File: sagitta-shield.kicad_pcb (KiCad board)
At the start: 2 copper layers, 29.2 x 91.6 mm, 53 parts, among them J1 EADC1, J10 SENSGND, J11 POWER, J2 EADC2, J3 MicroSD, J4 RTD, J5 IADC, J6 SWITCH, J7 UART2, J8 I2C, J9 SENSVDD, Q1 BSS84, U1 MAX31865, U2 ADS1115IDGS, U3 A1104LLHL

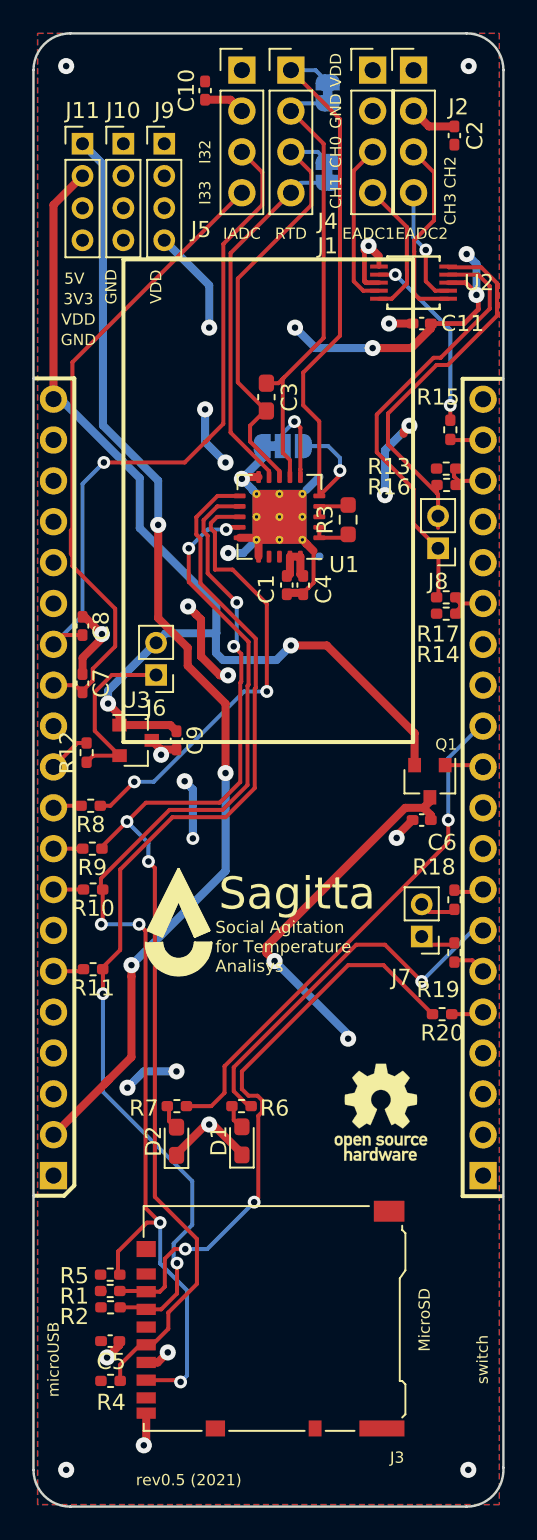
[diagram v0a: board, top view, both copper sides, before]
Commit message: fix previous version PCB's errors
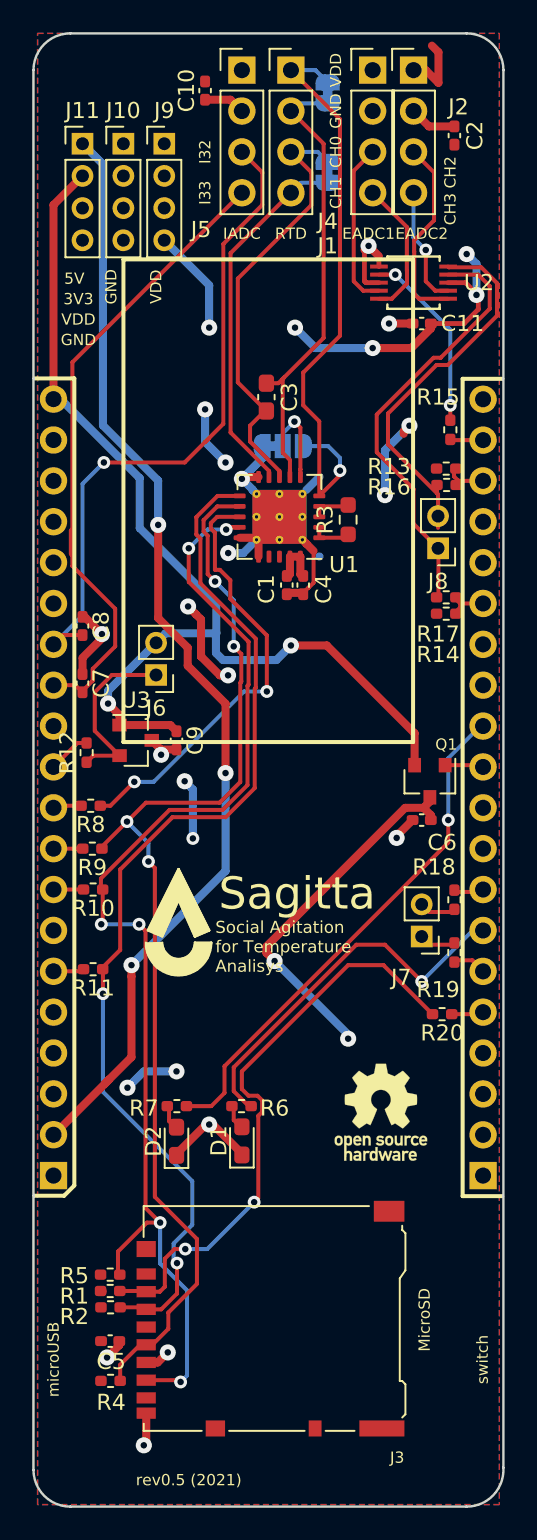
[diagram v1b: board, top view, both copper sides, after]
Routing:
- net VDD: track 68.7 -> 73.1 mm
- net GND: vias 17 -> 13
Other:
- net class Default removed
- net class Power removed
